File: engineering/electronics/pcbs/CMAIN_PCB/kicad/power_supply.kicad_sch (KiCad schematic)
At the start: 36 parts, among them Q101 N-MOSFET_LOW_RDS_ON_TBD, Q102 N-MOSFET_LOW_RDS_ON_TBD, Q103 N-MOSFET_LOW_RDS_ON_TBD, Q104 N-MOSFET_LOW_RDS_ON_TBD, Q105 N-MOSFET_LOW_RDS_ON_TBD, Q106 N-MOSFET_LOW_RDS_ON_TBD, U101 LTC4370xMS, U102 LTC4370xMS, U103 LTC4370xMS

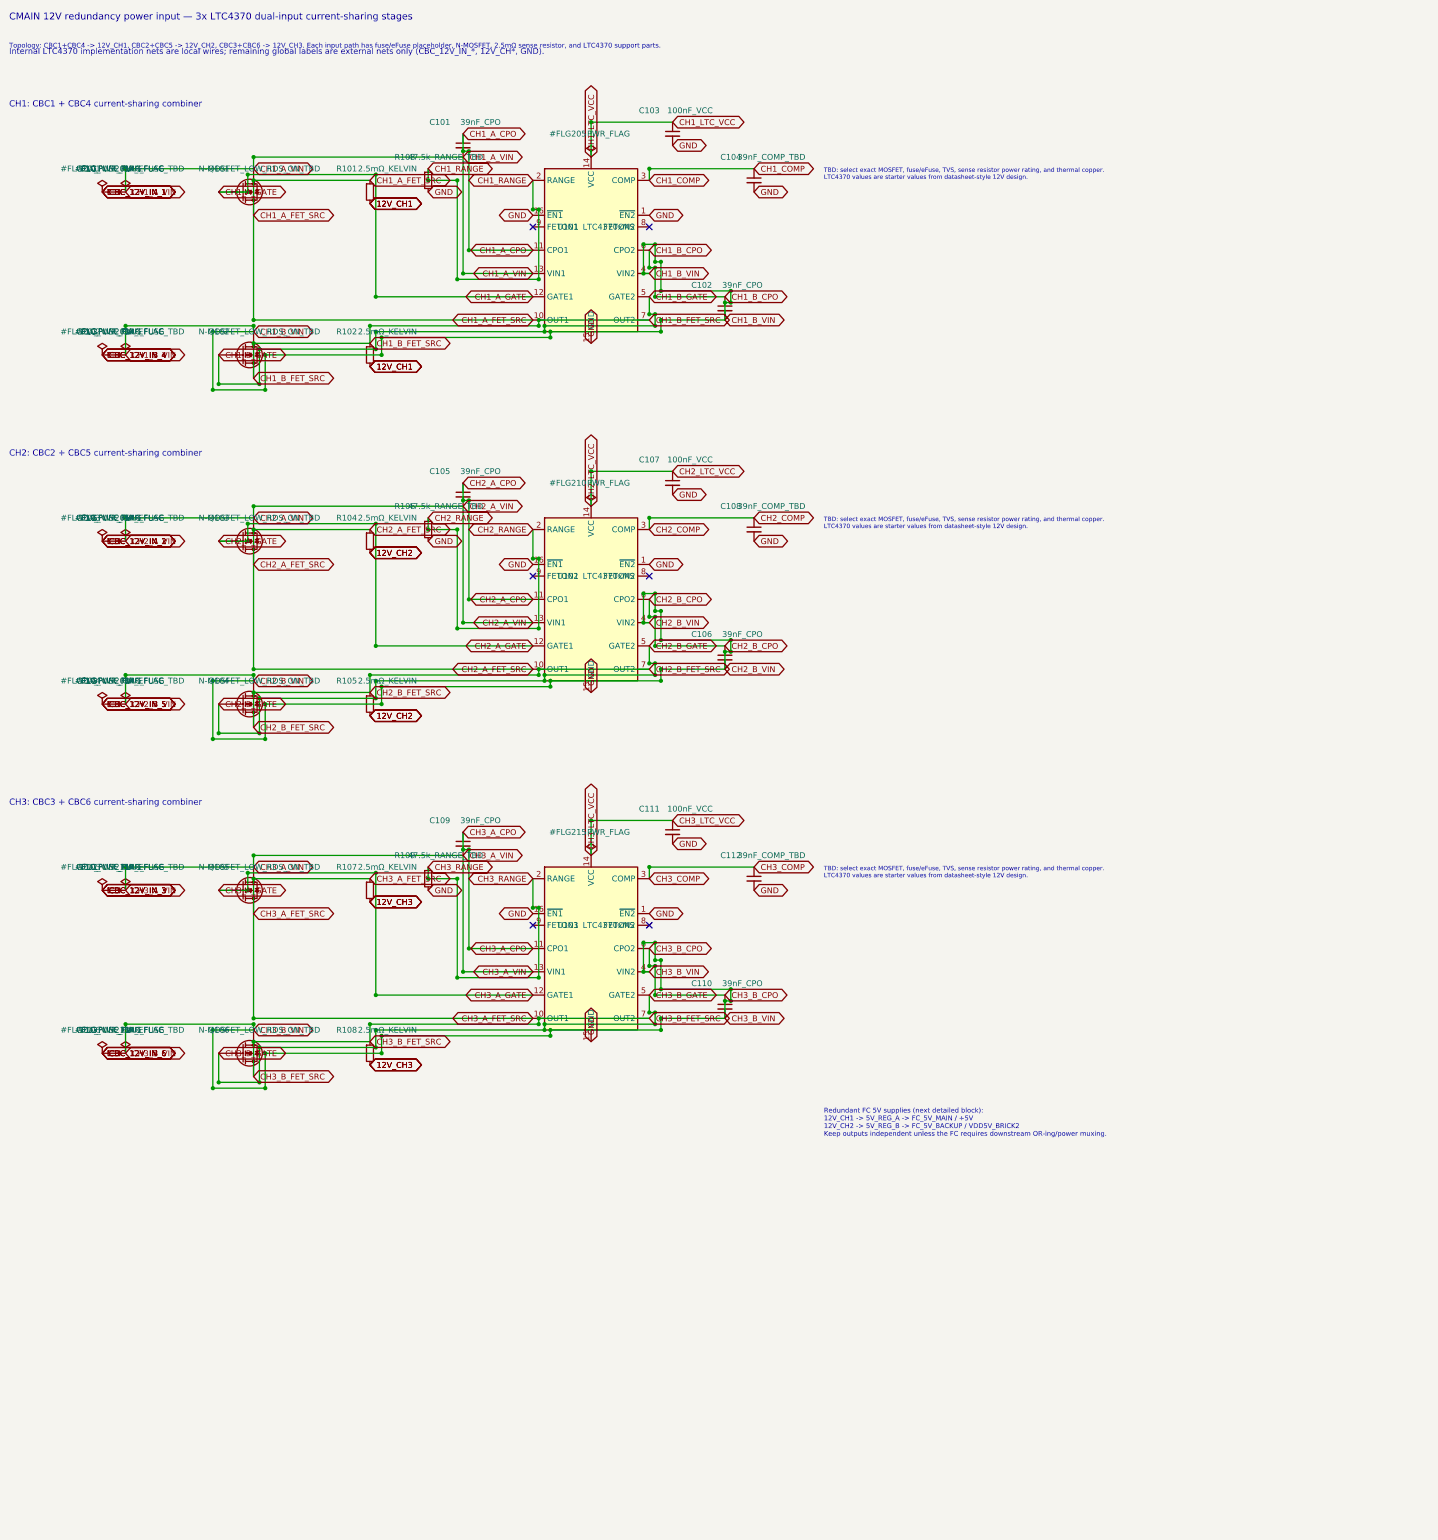
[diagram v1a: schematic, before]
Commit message: electronics: update CMAIN and CBC PCB files
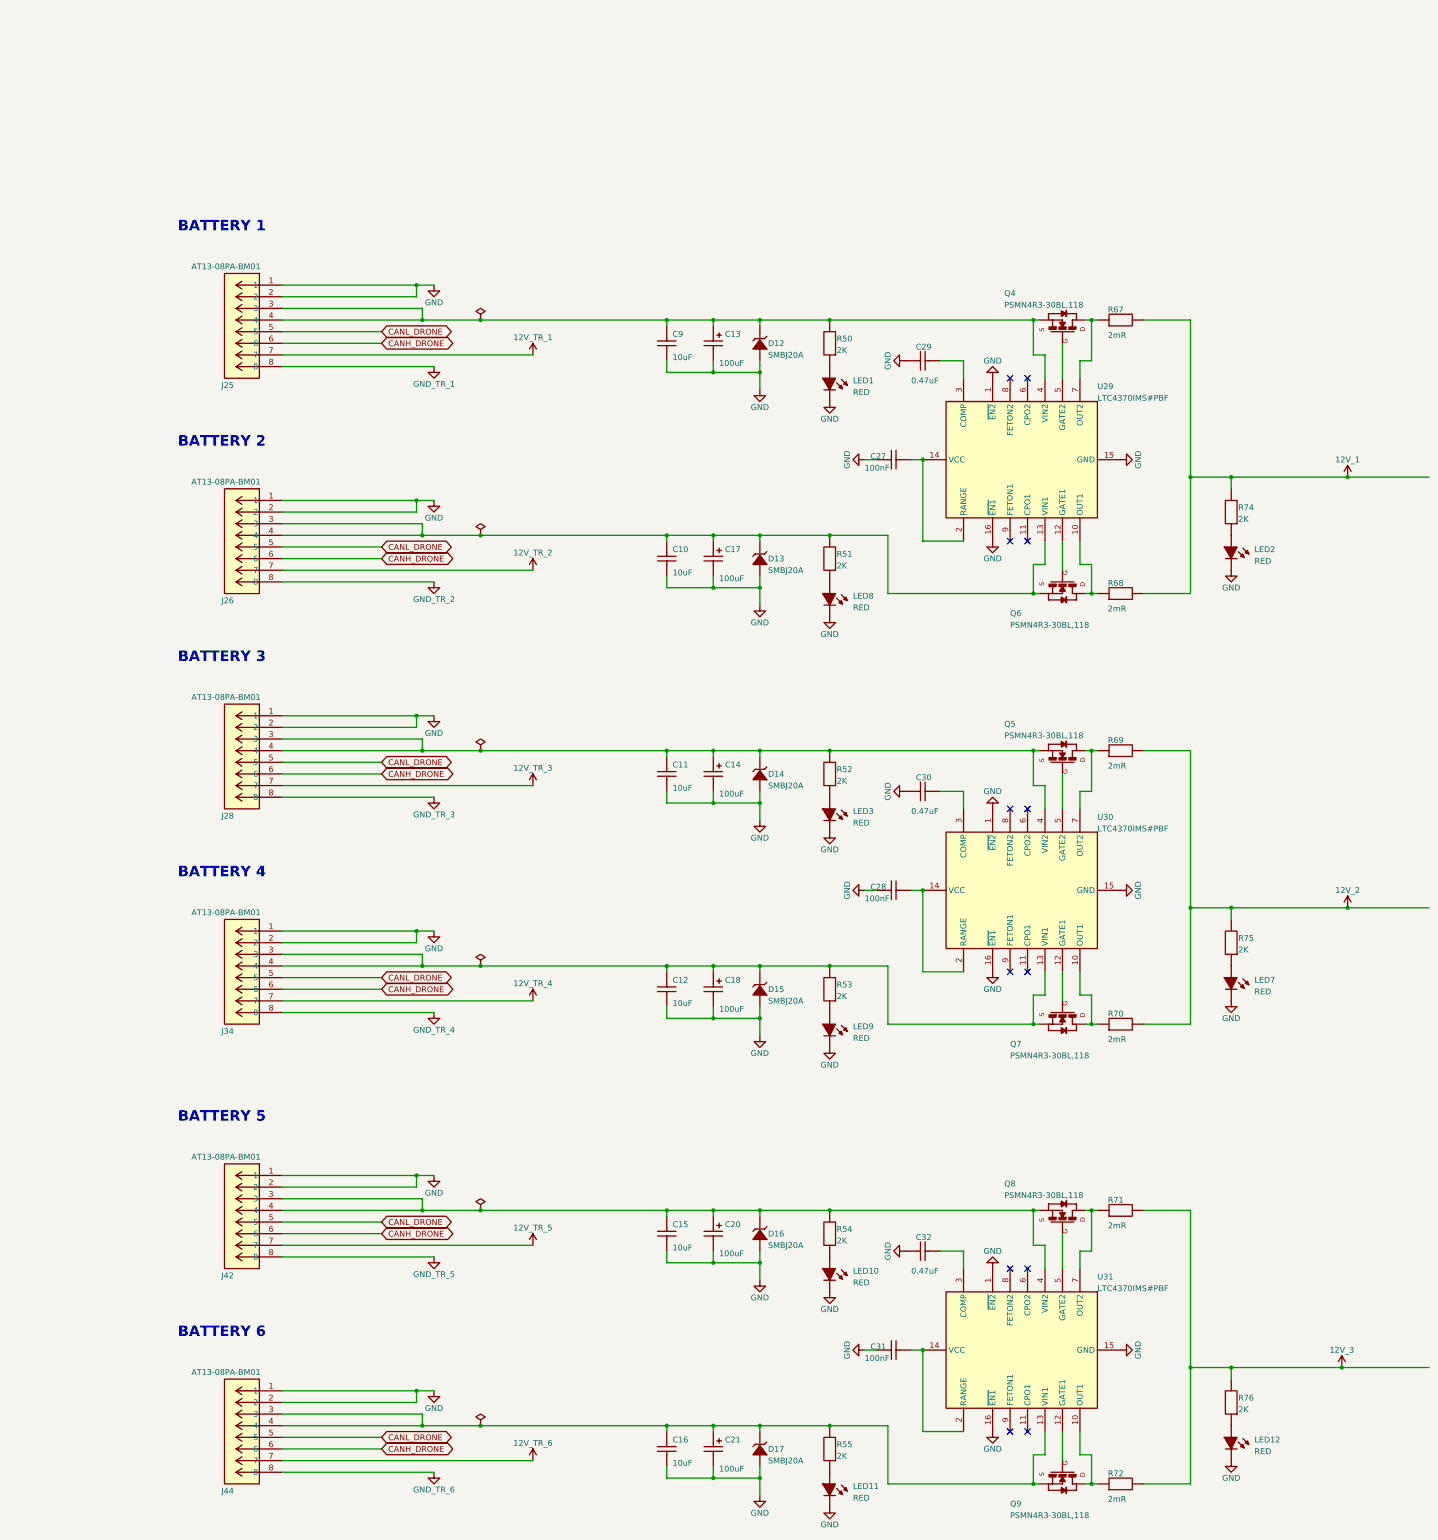
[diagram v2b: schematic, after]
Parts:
- removed C101, C102, C105, C106, C109, C110: 39nF_CPO, Capacitor_SMD:C_0603_1608Metric, symbol Device:C_Small
- removed C103, C107, C111: 100nF_VCC, Capacitor_SMD:C_0603_1608Metric, symbol Device:C_Small
- removed C104, C108, C112: 39nF_COMP_TBD, Capacitor_SMD:C_0603_1608Metric, symbol Device:C_Small
- removed F101, F102, F103, F104, F105, F106: 10A_FUSE_OR_EFUSE_TBD, symbol Device:Fuse_Small
- removed Q101, Q102, Q103, Q104, Q105, Q106: N-MOSFET_LOW_RDS_ON_TBD, symbol Device:Q_NMOS
- removed R101, R102, R104, R105, R107, R108: 2.5mΩ_KELVIN, Resistor_SMD:R_2512_6332Metric, symbol Device:R_Small
- removed R103, R106, R109: 47.5k_RANGE_TBD, Resistor_SMD:R_0805_2012Metric_Pad1.20x1.40mm_HandSolder, symbol Device:R_Small
- removed U101, U102, U103: LTC4370xMS, Package_SO:MSOP-16_3x4.039mm_P0.5mm, symbol Power_Management:LTC4370xMS
- added C10, C11, C12, C15, C16, C9: ${ALTIUM_VALUE}, C1206, symbol Signal Distribution Box-altium-import:root_1_10uF ± 10% 25V
- added C13, C14, C17, C18, C20, C21: ${ALTIUM_VALUE}, CAP_EEUFC1E101S, symbol Signal Distribution Box-altium-import:root_3_100uF ± 20% 25V_0
- added C27, C28, C31: ${ALTIUM_VALUE}, C0805, symbol Signal Distribution Box-altium-import:root_0_100nF ± 10% 50V
- added C29, C30, C32: ${ALTIUM_VALUE}, C0805, symbol Signal Distribution Box-altium-import:root_0_0.47uF ± 10% 50V
- added D12, D13, D14, D15, D16, D17: ${ALTIUM_VALUE}, DO-214AA2, symbol Signal Distribution Box-altium-import:root_2_SMBJ20A
- added J25, J26, J28, J34, J42, J44: ${ALTIUM_VALUE}, CBC_PCB:AT13-08PA-BM01, symbol CBC_PCB:AT13-08PA-BM01
- added LED1, LED10, LED11, LED12, LED2, LED3, LED7, LED8, LED9: ${ALTIUM_VALUE}, LED_PLCC2, symbol Signal Distribution Box-altium-import:root_3_LED_SMD
- added Q4, Q5, Q8: PSMN4R3-30BL,118, TRANS_PSMN4R8-100BSE, symbol Signal Distribution Box-altium-import:root_1_mirrored_PSMN4R3-30BL,118
- added Q6, Q7, Q9: ${ALTIUM_VALUE}, TRANS_PSMN4R8-100BSE, symbol Signal Distribution Box-altium-import:root_3_PSMN4R3-30BL,118
- added R50, R51, R52, R53, R54, R55, R74, R75, R76: ${ALTIUM_VALUE}, R0805, symbol Signal Distribution Box-altium-import:root_1_2 kOhms ±1% 0.125W
- added R67, R68, R69, R70, R71, R72: ${ALTIUM_VALUE}, R2512, symbol Signal Distribution Box-altium-import:root_0_2 mOhms ±1% 1W
- added U29, U30, U31: LTC4370IMS#PBF, SOP50P490X110-16N, symbol Signal Distribution Box-altium-import:root_1_LTC4370IMS#PBF
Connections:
- net GND: now also C10.1, C11.1, C12.1, C13.2, C14.2, C15.1, C16.1, C17.2, C18.2, C20.2, C21.2, C27.1, C28.1, C29.1, C30.1, C31.1, C32.1, C9.1, D12.A, D13.A, D14.A, D15.A, D16.A, D17.A, J25.1, J25.2, J26.1, J26.2, J28.1, J28.2, J34.1, J34.2, J42.1, J42.2, J44.1, J44.2, LED1.C, LED10.C, LED11.C, LED12.C, LED2.C, LED3.C, LED7.C, LED8.C, LED9.C, U29.1 (~{EN2}), U29.15 (GND), U29.16 (~{EN1}), U30.1 (~{EN2}), U30.15 (GND), U30.16 (~{EN1}), U31.1 (~{EN2}), U31.15 (GND), U31.16 (~{EN1})
- new net: Q7.1 (G), U30.12 (GATE1)
- new net: Q7.2 (D), R70.1, U30.10 (OUT1)
- new net: C12.2, C18.1, D15.C, J34.3, J34.4, Q7.3 (S), R53.2, U30.13 (VIN1)
- new net: Q8.2 (D), R71.1, U31.7 (OUT2)
- new net: Q4.2 (D), R67.1, U29.7 (OUT2)
- new net: C16.2, C21.1, D17.C, J44.3, J44.4, Q9.3 (S), R55.2, U31.13 (VIN1)
- new net: Q5.1 (G), U30.5 (GATE2)
- new net: Q5.2 (D), R69.1, U30.7 (OUT2)
- new net: C11.2, C14.1, D14.C, J28.3, J28.4, Q5.3 (S), R52.2, U30.4 (VIN2)
- new net: LED12.A, R76.1
- new net: LED10.A, R54.1
- new net: C15.2, C20.1, D16.C, J42.3, J42.4, Q8.3 (S), R54.2, U31.4 (VIN2)
- new net: LED3.A, R52.1
- new net: C28.2, U30.14 (VCC), U30.2 (RANGE)
- new net: Q9.2 (D), R72.1, U31.10 (OUT1)
- new net: C10.2, C17.1, D13.C, J26.3, J26.4, Q6.3 (S), R51.2, U29.13 (VIN1)
- new net: LED8.A, R51.1
- new net: Q4.1 (G), U29.5 (GATE2)
- new net: C13.1, C9.2, D12.C, J25.3, J25.4, Q4.3 (S), R50.2, U29.4 (VIN2)
- new net: C32.2, U31.3 (COMP)
- new net: C27.2, U29.14 (VCC), U29.2 (RANGE)
- new net: Q9.1 (G), U31.12 (GATE1)
- new net: LED11.A, R55.1
- new net: C30.2, U30.3 (COMP)
- new net: Q6.1 (G), U29.12 (GATE1)
- new net: Q6.2 (D), R68.1, U29.10 (OUT1)
- new net: LED9.A, R53.1
- new net: LED7.A, R75.1
- new net: C29.2, U29.3 (COMP)
- new net: LED1.A, R50.1
- new net: C31.2, U31.14 (VCC), U31.2 (RANGE)
- new net: Q8.1 (G), U31.5 (GATE2)
- new net: LED2.A, R74.1
- new net 12V_1: R67.2, R68.2, R74.2
- new net 12V_2: R69.2, R70.2, R75.2
- new net 12V_3: R71.2, R72.2, R76.2
- new net 12V_TR_1: J25.7
- new net 12V_TR_2: J26.7
- new net 12V_TR_3: J28.7
- new net 12V_TR_4: J34.7
- new net 12V_TR_5: J42.7
- new net 12V_TR_6: J44.7
- new net CANH_DRONE: J25.6, J26.6, J28.6, J34.6, J42.6, J44.6
- new net CANL_DRONE: J25.5, J26.5, J28.5, J34.5, J42.5, J44.5
- new net GND_TR_1: J25.8
- new net GND_TR_2: J26.8
- new net GND_TR_3: J28.8
- new net GND_TR_4: J34.8
- new net GND_TR_5: J42.8
- new net GND_TR_6: J44.8
- no-connect marks 6 -> 12
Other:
- note added: "BATTERY 1"
- note added: "BATTERY 2"
- note added: "BATTERY 3"
- note added: "BATTERY 4"
- note added: "BATTERY 5"
- note added: "BATTERY 6"
- note removed: "CH1: CBC1 + CBC4 current-sharing combiner"
- note removed: "CH2: CBC2 + CBC5 current-sharing combiner"
- note removed: "CH3: CBC3 + CBC6 current-sharing combiner"
- note removed: "CMAIN 12V redundancy power input — 3x LTC4370 dual-input current-sharing stages"
- note removed: "Internal LTC4370 implementation nets are local wires; remaining global labels are external nets only (CBC_12V_IN_*, 12V_CH*, GND)."
- note removed: "Redundant FC 5V supplies (next detailed block): 12V_CH1 -> 5V_REG_A -> FC_5V_MAIN / +5V 12V_CH2 -> 5V_REG_B -> FC_5V_BACKUP / VDD5V_BRICK2 Keep outputs independent unless the FC requires downstream OR-ing/power muxing."
- note removed: "TBD: select exact MOSFET, fuse/eFuse, TVS, sense resistor power rating, and thermal copper. LTC4370 values are starter values from datasheet-style 12V design."
- note removed: "Topology: CBC1+CBC4 -> 12V_CH1, CBC2+CBC5 -> 12V_CH2, CBC3+CBC6 -> 12V_CH3. Each input path has fuse/eFuse placeholder, N-MOSFET, 2.5mΩ sense resistor, and LTC4370 support parts."
